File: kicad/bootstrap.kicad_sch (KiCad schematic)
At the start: 3 parts, among them U5 74HC595, U6 74HC595

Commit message: v2.0
Production ready
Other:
- company: (none) -> Daniel Molina García
- title: (none) -> SBC6526 - RAM Bootstrap
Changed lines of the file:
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@@
 (kicad_sch (version 20201015) (generator eeschema)
   (paper "A4")
+  (title_block
+    (title "SBC6526 - RAM Bootstrap")
+    (date "2021-10-01")
+    (rev "2.0")
+    (company "Daniel Molina García")
+  )
   (junction (at 114.3 120.65) (diameter 1.016) (color 0 0 0 0))
   (junction (at 168.91 95.25) (diameter 1.016) (color 0 0 0 0))
@@
   (junction (at 179.07 74.93) (diameter 1.016) (color 0 0 0 0))
   (junction (at 181.61 77.47) (diameter 1.016) (color 0 0 0 0))
+  (no_connect (at 125.73 97.79))
+  (no_connect (at 212.09 139.7))
+  (no_connect (at 100.33 74.93))
+  (no_connect (at 110.49 64.77))
+  (no_connect (at 125.73 105.41))
+  (no_connect (at 125.73 74.93))
+  (no_connect (at 125.73 85.09))
   (no_connect (at 125.73 102.87))
-  (no_connect (at 110.49 64.77))
-  (no_connect (at 125.73 97.79))
-  (no_connect (at 125.73 85.09))
-  (no_connect (at 125.73 74.93))
-  (no_connect (at 212.09 139.7))
-  (no_connect (at 125.73 105.41))
+  (no_connect (at 115.57 64.77))
   (no_connect (at 125.73 77.47))
   (no_connect (at 100.33 77.47))
-  (no_connect (at 115.57 64.77))
-  (no_connect (at 100.33 74.93))
   (bus_entry (at 88.9 80.01) (size -2.54 -2.54)
     (stroke (width 0.1524) (type solid) (color 0 0 0 0))

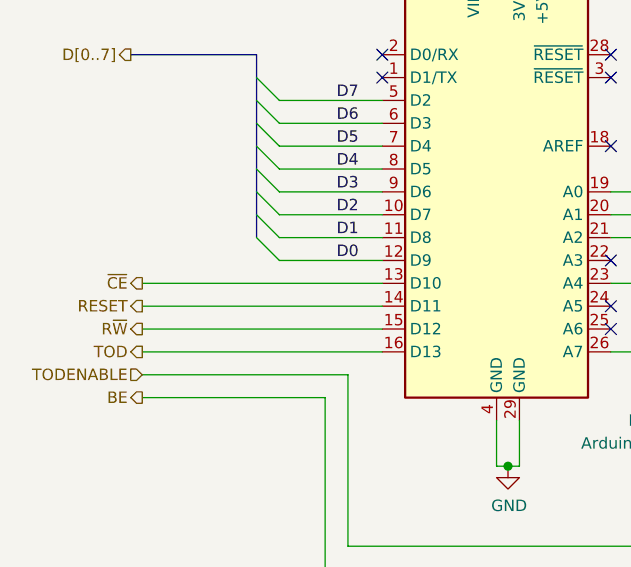
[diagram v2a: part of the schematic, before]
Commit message: Fixes
* Minor fixes to routing
* Right VCC hole was slightly offset. Fixed
* Removed /CE from arduino to RAM. As RAMCE pulses with PHI, it's not necessary, and we leave /CE tied to GND.
* Fixed RAM footprint, as it was too wide. Improved routing.
* Added current limiting resistor to LCD Contrast
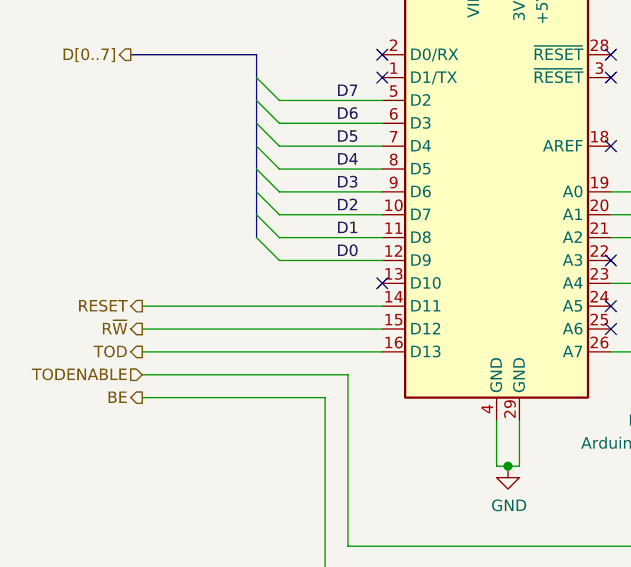
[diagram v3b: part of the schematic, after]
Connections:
- net ~CE: no longer names the net of NANO1.13 (D10)
- no-connect marks 11 -> 12
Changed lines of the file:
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@@
   (junction (at 179.07 74.93) (diameter 1.016) (color 0 0 0 0))
   (junction (at 181.61 77.47) (diameter 1.016) (color 0 0 0 0))
+  (no_connect (at 125.73 97.79))
+  (no_connect (at 100.33 77.47))
+  (no_connect (at 125.73 85.09))
+  (no_connect (at 100.33 100.33))
+  (no_connect (at 125.73 102.87))
+  (no_connect (at 125.73 74.93))
   (no_connect (at 115.57 64.77))
+  (no_connect (at 125.73 105.41))
+  (no_connect (at 125.73 77.47))
+  (no_connect (at 100.33 74.93))
+  (no_connect (at 212.09 139.7))
   (no_connect (at 110.49 64.77))
-  (no_connect (at 125.73 105.41))
-  (no_connect (at 100.33 74.93))
-  (no_connect (at 125.73 74.93))
-  (no_connect (at 125.73 85.09))
-  (no_connect (at 100.33 77.47))
-  (no_connect (at 125.73 77.47))
-  (no_connect (at 212.09 139.7))
-  (no_connect (at 125.73 97.79))
-  (no_connect (at 125.73 102.87))
   (bus_entry (at 88.9 80.01) (size -2.54 -2.54)
     (stroke (width 0.1524) (type solid) (color 0 0 0 0))
@@
   )
   (wire (pts (xy 100.33 97.79) (xy 88.9 97.79))
-    (stroke (width 0) (type solid) (color 0 0 0 0))
-  )
-  (wire (pts (xy 100.33 100.33) (xy 73.66 100.33))
     (stroke (width 0) (type solid) (color 0 0 0 0))
   )
@@
     (effects (font (size 1.27 1.27)) (justify right))
   )
-  (hierarchical_label "~CE" (shape output) (at 73.66 100.33 180)
-    (effects (font (size 1.27 1.27)) (justify right))
-  )

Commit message: Uploaded firmware v2.0.2
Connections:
- net R~W renamed R~{W}
